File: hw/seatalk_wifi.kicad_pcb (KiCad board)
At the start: 2 copper layers, 31 x 22 mm, 42 parts, among them Q1 2N7002, Q2 2N7002, SW1 SW_SPST, SW2 SW_SPST, U1 AP62300_SOT23-6, U2 ESP-12E, U3 MAX3221CPWR

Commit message: Schematic chenged to reflect the voltage of input caps.
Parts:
- R2: value 1000 -> 330
- R8: value 3.3K -> 1000
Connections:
- net /ROUT renamed /RIN
- net Net-(U2-GPIO14) renamed /TOUT
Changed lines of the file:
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@@
   (net 33 "/UART1_TXD")
   (net 34 "/GPIO15")
-  (net 35 "/ROUT")
-  (net 36 "Net-(U2-GPIO14)")
+  (net 35 "/RIN")
+  (net 36 "/TOUT")
   (net 37 "unconnected-(U2-GPIO5)")
   (net 38 "Net-(U2-GPIO16)")
@@
         (effects (font (size 1 1) (thickness 0.15)))
     )
-    (fp_text value "1000" (at 0 1.43 90) (layer "F.Fab")
+    (fp_text value "330" (at 0 1.43 90) (layer "F.Fab")
         (effects (font (size 1 1) (thickness 0.15)))
     )
@@
       (net 29 "/RXD") (pinfunction "RIN") (pintype "input"))
     (pad "9" smd rect locked (at 2.95 2.275) (size 1.5 0.45) (layers "F.Cu" "F.Paste" "F.Mask")
-      (net 35 "/ROUT") (pinfunction "ROUT") (pintype "output"))
+      (net 35 "/RIN") (pinfunction "ROUT") (pintype "output"))
     (pad "10" smd rect locked (at 2.95 1.625) (size 1.5 0.45) (layers "F.Cu" "F.Paste" "F.Mask")
       (net 32 "unconnected-(U3-~{INVALID})") (pinfunction "~{INVALID}") (pintype "output+no_connect"))
     (pad "11" smd rect locked (at 2.95 0.975) (size 1.5 0.45) (layers "F.Cu" "F.Paste" "F.Mask")
-      (net 36 "Net-(U2-GPIO14)") (pinfunction "DIN") (pintype "input"))
+      (net 36 "/TOUT") (pinfunction "DIN") (pintype "input"))
     (pad "12" smd rect locked (at 2.95 0.325) (size 1.5 0.45) (layers "F.Cu" "F.Paste" "F.Mask")
       (net 2 "+3V3") (pinfunction "FORCEON") (pintype "input"))
@@
         (effects (font (size 1 1) (thickness 0.15)))
     )
-    (fp_text value "3.3K" (at 0 1.43) (layer "F.Fab")
+    (fp_text value "1000" (at 0 1.43) (layer "F.Fab")
         (effects (font (size 1 1) (thickness 0.15)))
     )
@@
       (net 13 "/UART0_RXD") (pintype "passive"))
     (pad "2" smd rect (at 0.7875 0 180) (size 0.875 0.95) (layers "F.Cu" "F.Paste" "F.Mask")
-      (net 35 "/ROUT") (pintype "passive"))
+      (net 35 "/RIN") (pintype "passive"))
     (model "${KIMY3DMOD}/resistor_SMD.3dshapes/R_0603_1608Metric.wrl"
       (offset (xyz 0 0 0))
@@
       (net 38 "Net-(U2-GPIO16)") (pinfunction "GPIO16") (pintype "bidirectional"))
     (pad "5" smd rect (at -7.6 -4.5 90) (size 2.5 1) (layers "B.Cu" "B.Paste" "B.Mask")
-      (net 36 "Net-(U2-GPIO14)") (pinfunction "GPIO14") (pintype "bidirectional"))
+      (net 36 "/TOUT") (pinfunction "GPIO14") (pintype "bidirectional"))
     (pad "6" smd rect (at -7.6 -6.5 90) (size 2.5 1) (layers "B.Cu" "B.Paste" "B.Mask")
       (net 22 "/LED") (pinfunction "GPIO12") (pintype "bidirectional"))

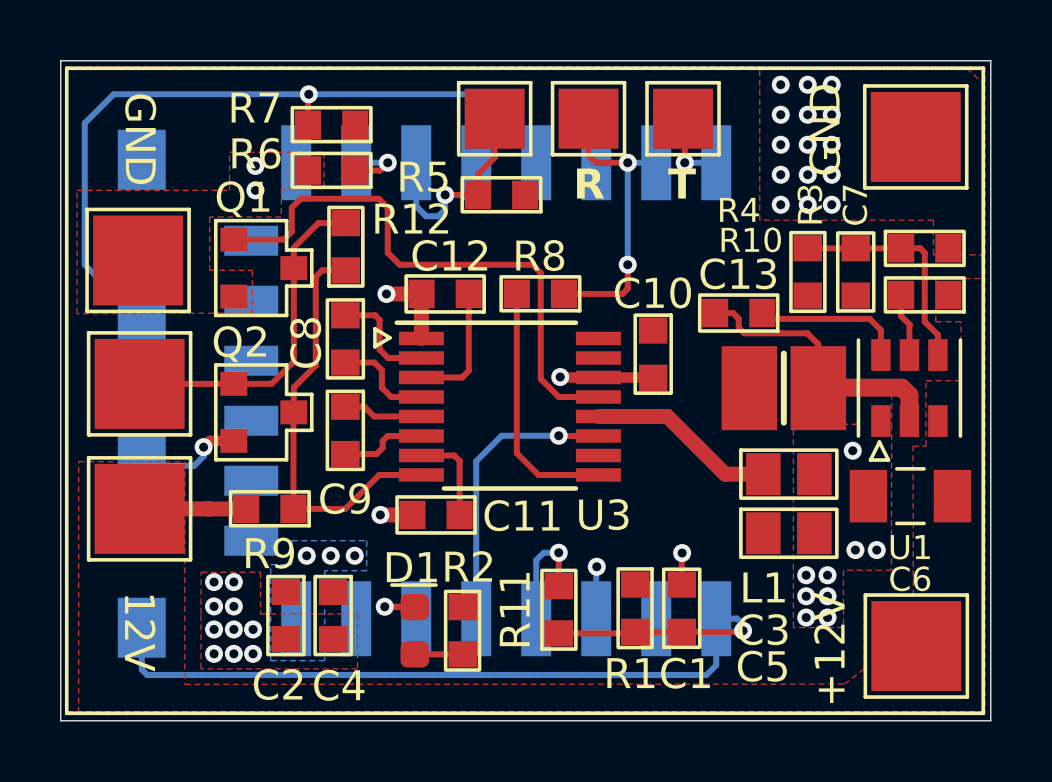
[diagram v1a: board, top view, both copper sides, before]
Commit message: Improvements to web page. SignalK integration. New holder design.
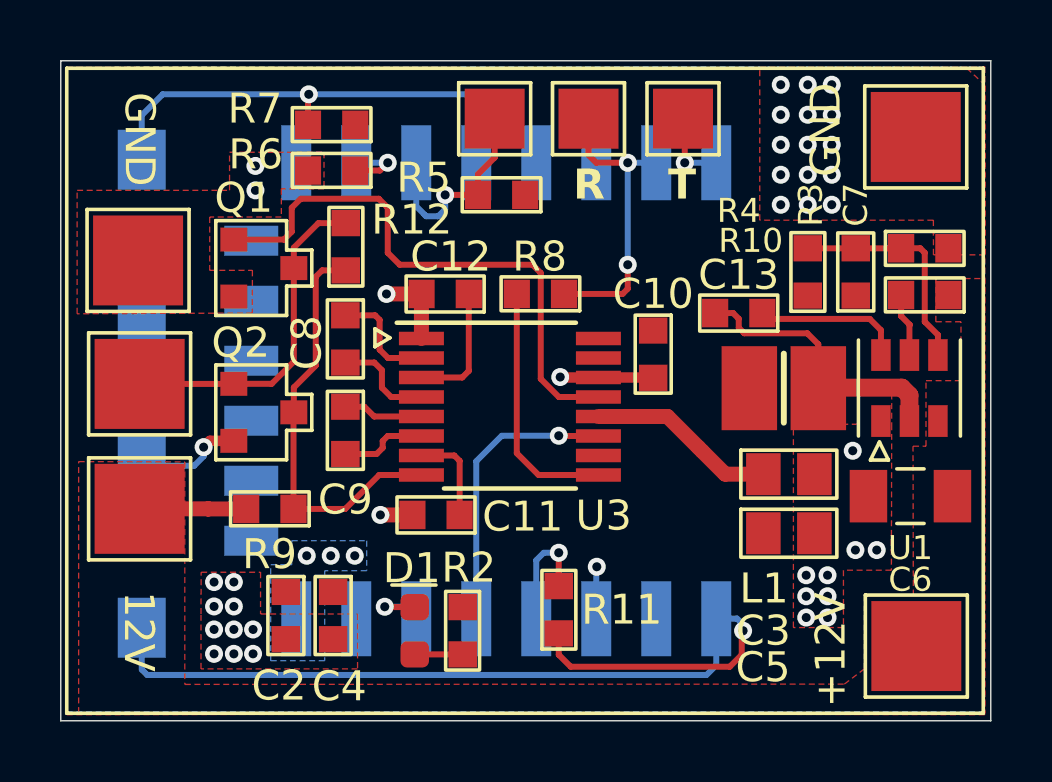
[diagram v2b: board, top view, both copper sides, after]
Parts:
- removed C1: 0.1uF, capacitor_SMD:C_0603_1608Metric
- removed R1: 10K, resistor_SMD:R_0603_1608Metric
- turned SW2 to 90 degrees
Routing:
- net /BOOT: track 23.2 -> 15.3 mm
- net GND: track 13.0 -> 10.4 mm, vias 41 -> 40
- net /~{RST}: track 29.7 -> 31.4 mm
- net /LED: track 2.22 -> 1.66 mm
